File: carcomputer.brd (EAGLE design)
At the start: 114 x 94.9 mm, 79 parts, among them IC1 LM358N, K1 351, K2 RT184012, K3 RT184012, Q1 BS170, Q5 TIP136, T1 BC618, T2 BC618, T3 BC618, T4 BC618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

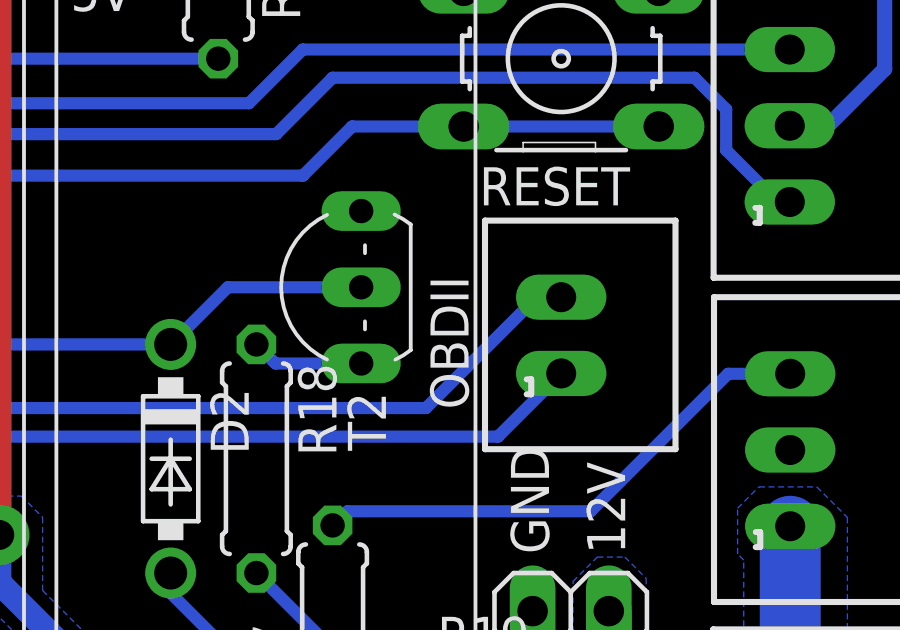
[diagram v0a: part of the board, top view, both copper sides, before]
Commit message: Renamed OBDII to CAN
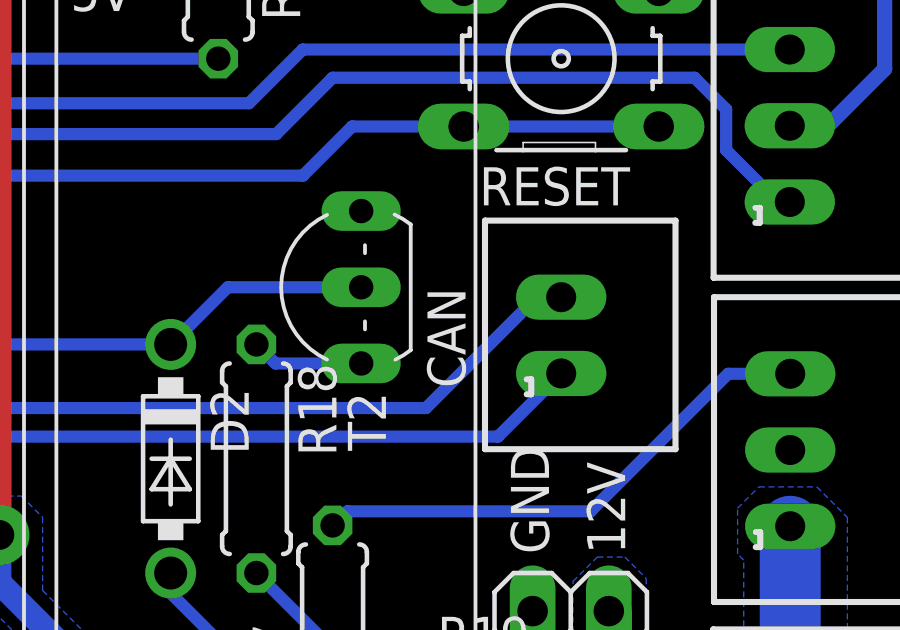
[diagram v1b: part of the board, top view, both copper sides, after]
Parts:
- renumbered OBDII to CAN
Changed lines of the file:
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@@
 <attribute name="VALUE" x="67.31" y="77.47" size="1.27" layer="27"/>
 </element>
-<element name="OBDII" library="con-jst-custom" package="B2B-ZR2.5" value="2.52B-ZR" x="89.2175" y="14.9225" smashed="yes" rot="R90">
-<attribute name="NAME" x="86.13" y="12.4425" size="1.27" layer="25" rot="R90"/>
+<element name="CAN" library="con-jst-custom" package="B2B-ZR2.5" value="2.52B-ZR" x="89.2175" y="14.9225" smashed="yes" rot="R90">
+<attribute name="NAME" x="86.0284" y="13.1537" size="1.27" layer="25" rot="R90"/>
 <attribute name="VALUE" x="92.7175" y="11.1725" size="1.27" layer="27" rot="R90"/>
 </element>
@@
 <signal name="CAN_H">
 <contactref element="U$2" pad="CAN_H"/>
-<contactref element="OBDII" pad="2"/>
+<contactref element="CAN" pad="2"/>
 <wire x1="84.7097" y1="12.4841" x2="64.8716" y2="12.4841" width="0.4064" layer="16"/>
 <wire x1="64.8716" y1="12.4841" x2="56.1975" y2="3.81" width="0.4064" layer="16"/>
@@
 <signal name="CAN_L">
 <contactref element="U$2" pad="CAN_L"/>
-<contactref element="OBDII" pad="1"/>
+<contactref element="CAN" pad="1"/>
 <wire x1="87.1114" y1="11.5316" x2="66.4591" y2="11.5316" width="0.4064" layer="16"/>
 <wire x1="66.4591" y1="11.5316" x2="58.7375" y2="3.81" width="0.4064" layer="16"/>

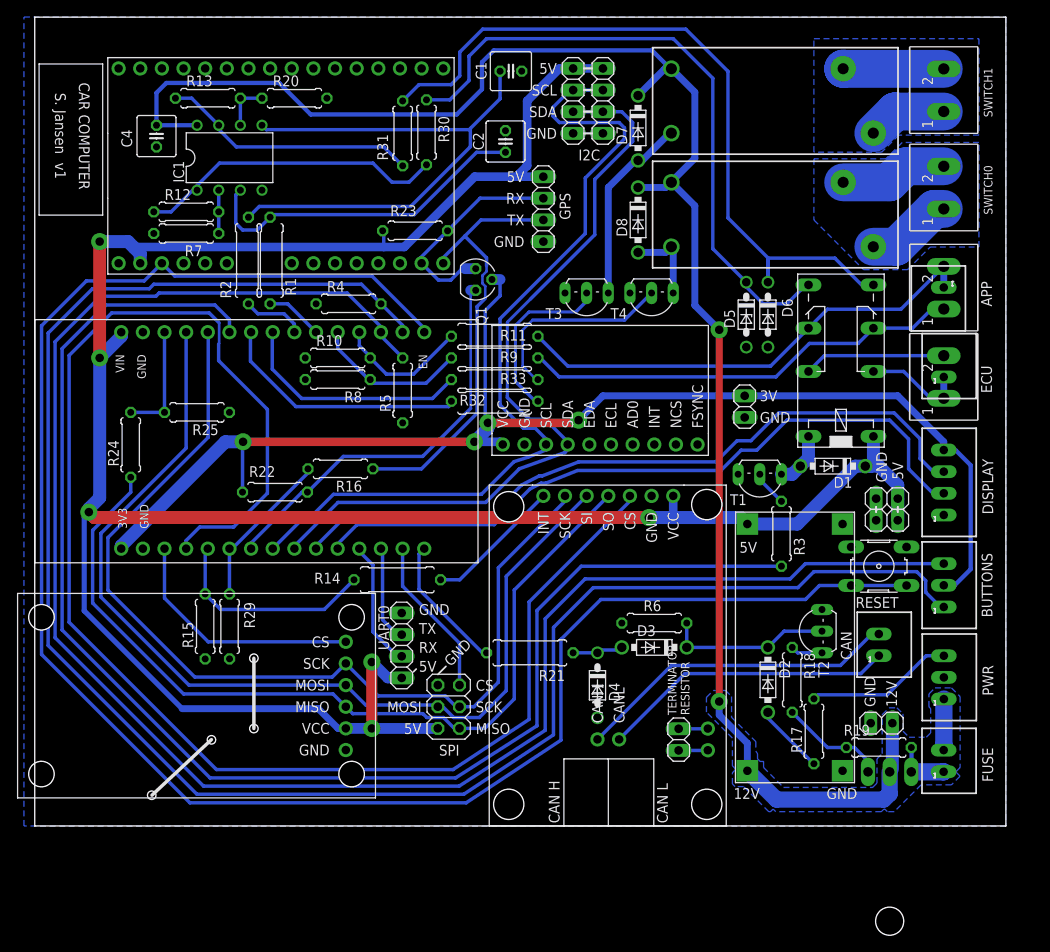
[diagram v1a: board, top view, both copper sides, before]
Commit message: Repositioned labels to make them more clear. Also added pin labels to connectors.
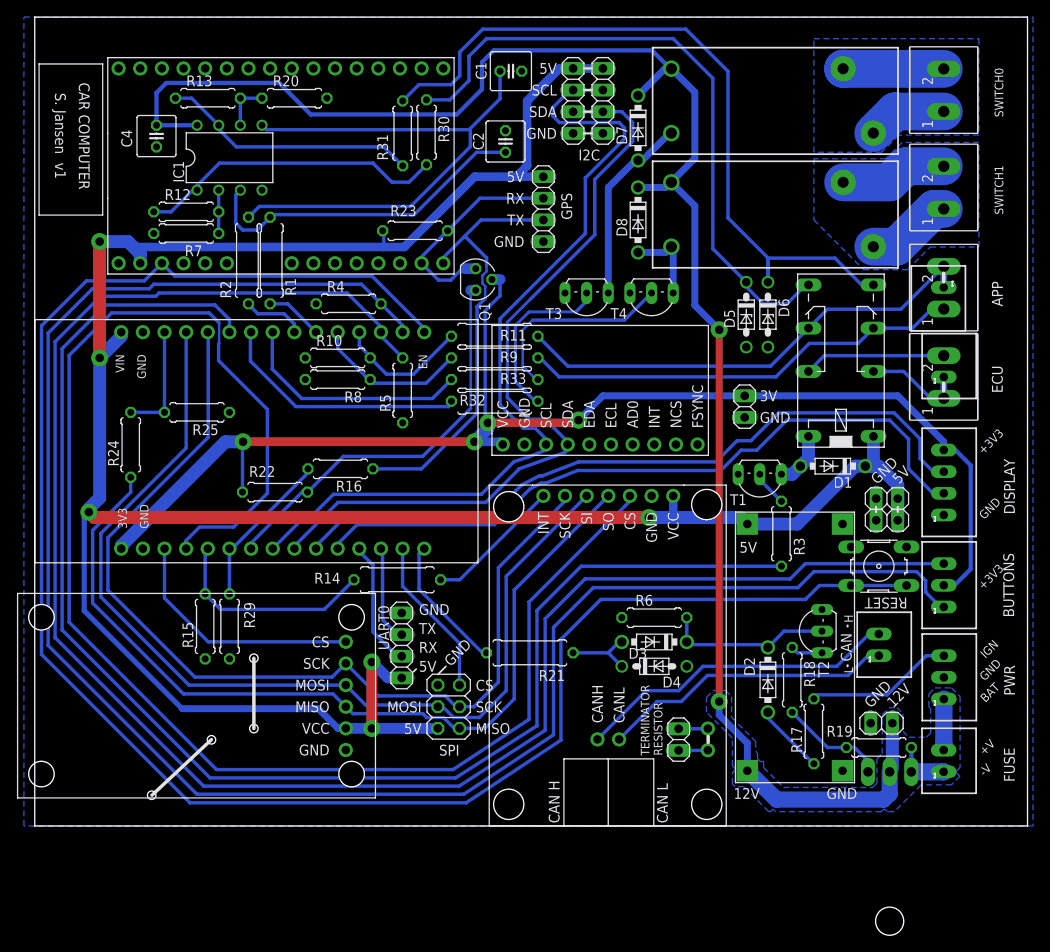
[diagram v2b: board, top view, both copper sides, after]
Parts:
- moved D4 7.03 mm to (62.9, 12.4), turned to 0 degrees
- moved R6 0.64 mm to (62.9, 18.1)
- moved D3 0.63 mm to (62.9, 15.2)
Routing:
- net N$11: track 5.98 -> 8.49 mm
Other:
- board size 114 x 94.9 mm -> 116.5 x 94.9 mm
- board text added: "+3V3"
- board text added: "+V"
- board text added: "-V"
- board text added: "BAT"
- board text added: "H"
- board text added: "IGN"
- board text added: "L"
